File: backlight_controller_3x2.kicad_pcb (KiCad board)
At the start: 2 copper layers, 70.5 x 41.9 mm, 1 part

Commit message: Initial layout.
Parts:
- added C1: 0.1uF, backlight_controller_3x2:SM1210, B.Cu at (134.6, 102.9)
- added C2: 0.1uF, backlight_controller_3x2:SM1210, B.Cu at (125.1, 88.9)
- added C3: 0.1uF, backlight_controller_3x2:SM1210, B.Cu at (112.4, 92.7)
- added C4: 0.1uF, backlight_controller_3x2:SM1210, B.Cu at (104.8, 92.7)
- added C5: 0.1uF, backlight_controller_3x2:SM1210, B.Cu at (97.2, 92.7)
- added C6: 0.1uF, backlight_controller_3x2:SM1210, B.Cu at (89.5, 92.7)
- added D1: diode_schottky_45V_10A, backlight_controller_3x2:CFP15, B.Cu at (104.8, 75.6)
- added HPS1: BTS3256, backlight_controller_3x2:PG-TO252-5-11, B.Cu at (112.4, 89.5)
- added HPS2: BTS3256, backlight_controller_3x2:PG-TO252-5-11, B.Cu at (104.8, 89.5)
- added HPS3: BTS3256, backlight_controller_3x2:PG-TO252-5-11, B.Cu at (97.2, 89.5)
- added HPS4: BTS3256, backlight_controller_3x2:PG-TO252-5-11, B.Cu at (89.5, 89.5)
- added J1: DB9F_SMD, footprints:DB9F_SMD, F.Cu at (101.1, 88.9)
- added J2: DB9M_SMD, footprints:DB9M_SMD, F.Cu at (119.9, 88.9)
- added J3: M12-5_RCPT_F, backlight_controller_3x2:M12-5_RCPT_F, F.Cu at (151.8, 72.4)
- added J4: M12-5_RCPT_F, backlight_controller_3x2:M12-5_RCPT_F, F.Cu at (151.8, 105.4)
- added L1: LED_24V_RED, backlight_controller_3x2:LED_555-3XXX_R, F.Cu at (134.6, 88.9)
- added L10: LED_5V_GRN, backlight_controller_3x2:LED_555-3XXX_G, F.Cu at (141.6, 72.4)
- added L11: LED_5V_GRN, backlight_controller_3x2:LED_555-3XXX_G, F.Cu at (141.6, 105.4)
- added L2: LED_5V_GRN, backlight_controller_3x2:LED_555-3XXX_G, F.Cu at (134.6, 99.1)
- added L3: LED_5V_GRN, backlight_controller_3x2:LED_555-3XXX_G, F.Cu at (134.6, 96.5)
- added L4: LED_5V_GRN, backlight_controller_3x2:LED_555-3XXX_G, F.Cu at (134.6, 94.0)
- added L5: LED_5V_GRN, backlight_controller_3x2:LED_555-3XXX_G, F.Cu at (134.6, 91.4)
- added L6: LED_5V_GRN, backlight_controller_3x2:LED_555-3XXX_G, F.Cu at (134.6, 86.4)
- added L7: LED_5V_GRN, backlight_controller_3x2:LED_555-3XXX_G, F.Cu at (134.6, 83.8)
- added L8: LED_5V_GRN, backlight_controller_3x2:LED_555-3XXX_G, F.Cu at (134.6, 81.3)
- added L9: LED_5V_GRN, backlight_controller_3x2:LED_555-3XXX_G, F.Cu at (134.6, 78.7)
- added P1: MINI_FIT_JR_02X03_M_RA, backlight_controller_3x2:MINI-FIT-JR_02X03_M_RA, F.Cu at (153.7, 88.9)
- added R1: 5.9k, backlight_controller_3x2:SM1210, B.Cu at (112.4, 97.2)
- added R2: 5.9k, backlight_controller_3x2:SM1210, B.Cu at (104.8, 97.2)
- added R3: 5.9k, backlight_controller_3x2:SM1210, B.Cu at (97.2, 97.2)
- added R4: 5.9k, backlight_controller_3x2:SM1210, B.Cu at (89.5, 97.2)
- added R5: 140, backlight_controller_3x2:SM1210, B.Cu at (142.9, 81.3)
- added R6: 140, backlight_controller_3x2:SM1210, B.Cu at (142.9, 78.1)
- added R7: 140, backlight_controller_3x2:SM1210, B.Cu at (136.5, 74.3)
- added R8: 140, backlight_controller_3x2:SM1210, B.Cu at (136.5, 71.1)
- added U1: SN74ABT541BDWR, backlight_controller_3x2:SOIC_20, B.Cu at (125.1, 97.8)
- added U2: SN74ABT541BDWR, backlight_controller_3x2:SOIC_20, B.Cu at (125.1, 80.0)
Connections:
- MDB1 pad 14: (no net) -> /CHANNEL_4
- MDB1 pad 15: (no net) -> /CHANNEL_5
- MDB1 pad 16: (no net) -> /CHANNEL_6
- MDB1 pad 17: (no net) -> /CHANNEL_7
- MDB1 pad 18: (no net) -> /CHANNEL_8
- MDB1 pad 19: (no net) -> /CHANNEL_9
- MDB1 pad 2: (no net) -> /~ENABLE
- MDB1 pad 3: (no net) -> /CHANNEL_0
- MDB1 pad 4: (no net) -> /CHANNEL_1
- MDB1 pad 5: (no net) -> /CHANNEL_2
- MDB1 pad 6: (no net) -> /CHANNEL_3
- MDB1 pad GND: (no net) -> GND
- MDB1 pad VDD: (no net) -> VDD
- MDB1 pad VEE: (no net) -> VEE
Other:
- net class GND: trace_width 0.4064 -> 0.8128
- net class LEDPOWER: trace_width 0.6096 -> 0.4064
- board text added: "Janelia Modular Device backlight_controller part_number: 1271 09/2018 ver 1.0 3x2"
- board text removed: "Janelia Modular Device backlight_controller part_number: 1001 02/2017 ver 1.0 3x2"

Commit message: Finished version 1.0.
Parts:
- moved R5 27.0 mm to (135.9, 107.3), turned to 180 degrees
- moved R6 26.3 mm to (135.9, 103.5), turned to 180 degrees
- moved C1 19.8 mm to (120.7, 88.9), turned to 0 degrees
- moved L1 10.8 mm to (142.2, 96.5), turned to 270 degrees
- moved L10 8.64 mm to (134.6, 77.5), turned to 90 degrees
- moved L11 8.64 mm to (134.6, 100.3), turned to 90 degrees
- moved C2 1.91 mm to (127.0, 88.9)
- moved L4 1.27 mm to (134.6, 92.7)
- moved L7 1.27 mm to (134.6, 85.1)
- moved L9 1.27 mm to (134.6, 80.0)
- moved L2 1.27 mm to (134.6, 97.8)
- moved L3 1.27 mm to (134.6, 95.2)
- moved L5 1.27 mm to (134.6, 90.2)
- moved L6 1.27 mm to (134.6, 87.6)
- moved L8 1.27 mm to (134.6, 82.5)
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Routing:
- net GND: track 0.00 -> 283.2 mm, vias 0 -> 2
- net VAA: track 0.00 -> 149.3 mm, vias 0 -> 1
- net /~ENABLE: track 0.00 -> 117.9 mm
- net /CHANNEL_1: track 0.00 -> 91.2 mm
- net VDD: track 0.00 -> 84.8 mm
- net /CHANNEL_0: track 0.00 -> 70.1 mm, vias 0 -> 1
- net VEE: track 0.00 -> 69.2 mm
- net /CHANNEL_3: track 0.00 -> 67.1 mm, vias 0 -> 1
- net /CHANNEL_2: track 0.00 -> 67.1 mm, vias 0 -> 1
- net /backlight_3x2/C_3: track 0.00 -> 55.9 mm, vias 0 -> 1
- net /backlight_3x2/C_9: track 0.00 -> 54.3 mm, vias 0 -> 1
- net /backlight_3x2/low_power_outputs/OUTPUT_1: track 0.00 -> 54.0 mm, vias 0 -> 1
- net /backlight_3x2/low_power_outputs/OUTPUT_0: track 0.00 -> 52.7 mm, vias 0 -> 1
- net /backlight_3x2/C_2: track 0.00 -> 45.9 mm, vias 0 -> 1
- net /backlight_3x2/C_8: track 0.00 -> 39.8 mm
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- added copper zone on B.Cu, net GND
- added copper zone on F.Cu, net VAA
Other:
- net class LEDPOWER: clearance 0.254 -> 0.1016; trace_width 0.4064 -> 0.254; via_dia 0.889 -> 0.635; via_drill 0.635 -> 0.381
- net class POWER: clearance 0.254 -> 0.1016; trace_width 0.8128 -> 0.4064
- net class SIGNAL: trace_width 0.4064 -> 0.2032; via_dia 0.889 -> 0.635; via_drill 0.635 -> 0.381
- net class SUPERPOWER: clearance 0.254 -> 0.1016; trace_width 1.2192 -> 0.8128
- rule trace_min: 0.254 -> 0.2032
- rule via_min_drill: 0.508 -> 0.2032
- rule via_min_size: 0.889 -> 0.508
- board text added: "0"
- board text added: "1"
- board text added: "2"
- board text added: "3"
- board text added: "4"
- board text added: "5"
- board text added: "6"
- board text added: "7"
- board text added: "8"
- board text added: "9"
- board text added: "High Power Channels"
- board text added: "IR Backlight"
- board text added: "Low Power Channels"
- board text added: "Visible Backlight"

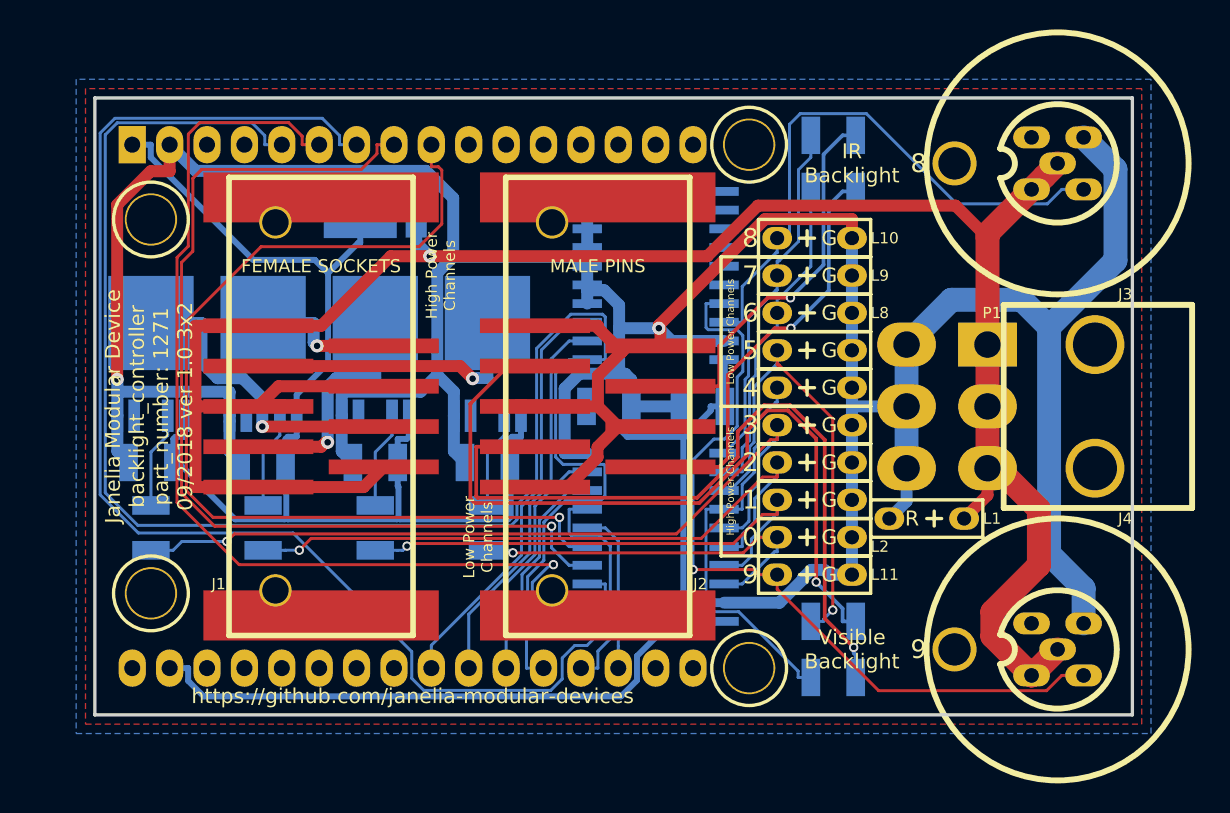
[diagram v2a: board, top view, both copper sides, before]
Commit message: Moved some pcb text.
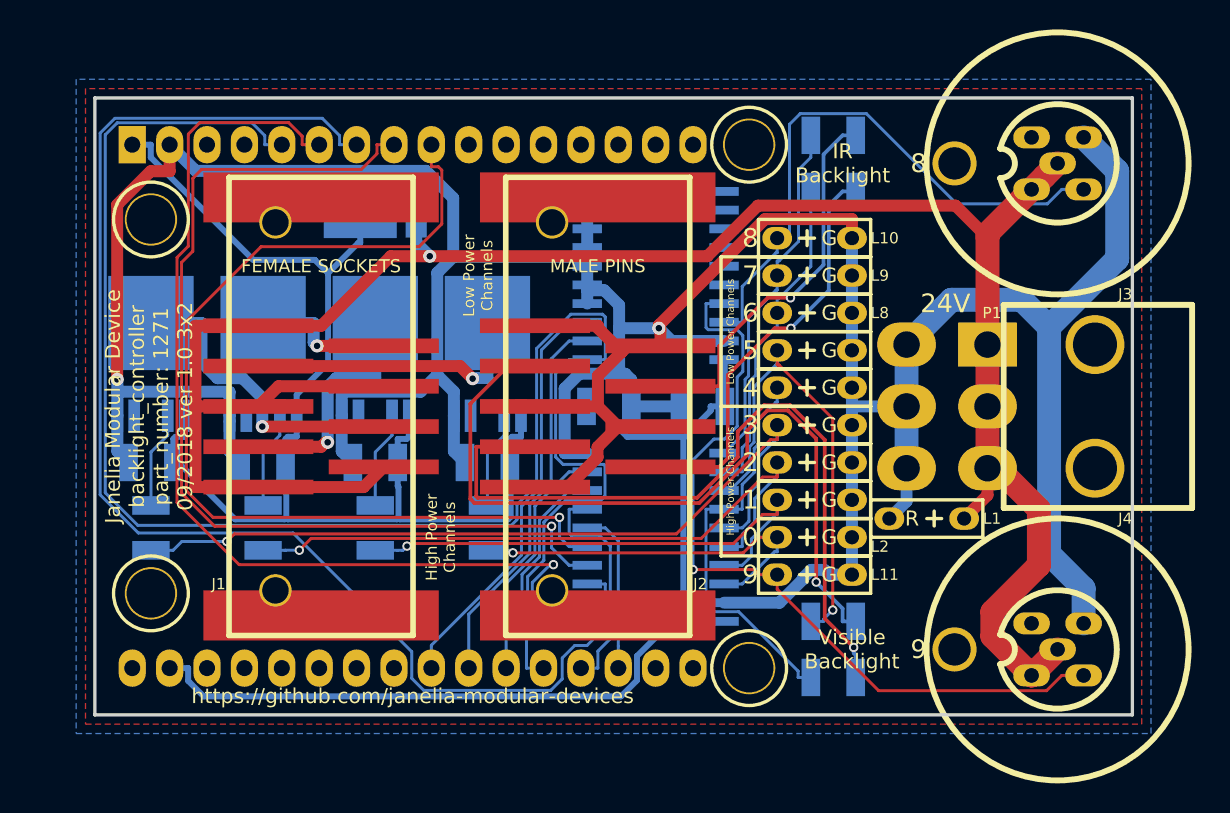
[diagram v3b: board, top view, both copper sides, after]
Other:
- board text added: "24V"
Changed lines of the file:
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@@
-(kicad_pcb (version 20171130) (host pcbnew 6.0.0-rc1-unknown-ba8647f~66~ubuntu18.04.1)
+(kicad_pcb (version 20171130) (host pcbnew 6.0.0-rc1-unknown-ab92882~66~ubuntu18.04.1)
   (general
     (thickness 1.6)
-    (drawings 28)
+    (drawings 29)
     (tracks 601)
     (zones 0)
@@
       (net 1 VEE) (solder_mask_margin 0.07) (clearance 0.07))
   )
+  (gr_text 24V (at 143.51 81.915) (layer F.SilkS)
+    (effects (font (size 1.27 1.27) (thickness 0.3175)))
+  )
   (gr_text "Visible\nBacklight" (at 137.16 105.41) (layer F.SilkS)
     (effects (font (size 1.016 1.016) (thickness 0.254)))
   )
-  (gr_text "IR\nBacklight" (at 137.16 72.39) (layer F.SilkS)
+  (gr_text "IR\nBacklight" (at 136.525 72.39) (layer F.SilkS)
     (effects (font (size 1.016 1.016) (thickness 0.254)))
   )
-  (gr_text "Low Power\nChannels" (at 111.76 97.79 90) (layer F.SilkS)
+  (gr_text "Low Power\nChannels" (at 111.76 80.01 90) (layer F.SilkS)
     (effects (font (size 0.762 0.762) (thickness 0.1905)))
   )
-  (gr_text "High Power\nChannels" (at 109.22 80.01 90) (layer F.SilkS)
+  (gr_text "High Power\nChannels" (at 109.22 97.79 90) (layer F.SilkS)
     (effects (font (size 0.762 0.762) (thickness 0.1905)))
   )
@@
   (segment (start 152.8978 70.6222) (end 152.898 70.6222) (width 0.8128) (layer B.Cu) (net 2))
   (segment (start 152.8978 103.6422) (end 152.898 103.642) (width 0.8128) (layer B.Cu) (net 2))
-  (segment (start 152.898 70.6222) (end 155.062 72.7866) (width 1.6256) (layer B.Cu) (net 2))
-  (segment (start 155.062 72.7866) (end 155.062 78.9945) (width 1.6256) (layer B.Cu) (net 2))
-  (segment (start 155.062 78.9945) (end 150.552 83.5051) (width 1.6256) (layer B.Cu) (net 2))
   (segment (start 119.175 79.375) (end 119.175 80.645) (width 0.8128) (layer B.Cu) (net 2))
   (segment (start 137.16 82.55) (end 137.16 85.09) (width 0.8128) (layer B.Cu) (net 2))
@@
   (via (at 124.0413 83.5869) (size 0.889) (layers F.Cu B.Cu) (net 2))
   (via (at 87.2428 87.0621) (size 0.889) (layers F.Cu B.Cu) (net 2))
+  (segment (start 155.18129 78.87581) (end 150.552 83.5051) (width 1.6256) (layer B.Cu) (net 2))
+  (segment (start 152.898 70.6222) (end 155.18129 72.90549) (width 1.6256) (layer B.Cu) (net 2))
+  (segment (start 155.18129 72.90549) (end 155.18129 78.87581) (width 1.6256) (layer B.Cu) (net 2))
   (segment (start 98.7302 96.4696) (end 98.7302 94.3614) (width 0.4064) (layer B.Cu) (net 3))
   (segment (start 98.7302 94.3614) (end 98.679 94.3102) (width 0.4064) (layer B.Cu) (net 3))

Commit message: Changes towards v1.1.
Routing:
- net GND: track 283.3 -> 0.00 mm, vias 2 -> 0
- net VAA: track 149.3 -> 0.00 mm, vias 1 -> 0
- net /~ENABLE: track 117.9 -> 0.00 mm
- net /CHANNEL_1: track 91.2 -> 0.00 mm
- net VDD: track 84.8 -> 0.00 mm
- net /CHANNEL_0: track 70.1 -> 0.00 mm, vias 1 -> 0
- net VEE: track 69.2 -> 0.00 mm
- net /CHANNEL_3: track 67.1 -> 0.00 mm, vias 1 -> 0
- net /CHANNEL_2: track 67.1 -> 0.00 mm, vias 1 -> 0
- net /backlight_3x2/C_3: track 55.9 -> 0.00 mm, vias 1 -> 0
- net /backlight_3x2/C_9: track 54.3 -> 0.00 mm, vias 1 -> 0
- net /backlight_3x2/low_power_outputs/OUTPUT_1: track 54.0 -> 0.00 mm, vias 1 -> 0
- net /backlight_3x2/low_power_outputs/OUTPUT_0: track 52.7 -> 0.00 mm, vias 1 -> 0
- net /backlight_3x2/C_2: track 45.9 -> 0.00 mm, vias 1 -> 0
- net /backlight_3x2/C_8: track 39.8 -> 0.00 mm
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- removed copper zone on B.Cu, net GND
- removed copper zone on F.Cu, net VAA
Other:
- board text added: "Janelia Modular Device backlight_controller part_number: 1271 10/2018 ver 1.1 3x2"
- board text removed: "Janelia Modular Device backlight_controller part_number: 1271 09/2018 ver 1.0 3x2"

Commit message: Finished version 1.1.
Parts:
- added U3: NUD3124, backlight_controller_3x2:TO-236-3, B.Cu at (148.6, 75.6)
- added U4: NUD3124, backlight_controller_3x2:TO-236-3, B.Cu at (148.6, 102.2)
- J3, J4: value M12-5_RCPT_F -> M12-5-RCPT_F_SMD; footprint backlight_controller_3x2:M12-5_RCPT_F -> footprints:M12-5_RCPT_F_SMD
- moved J3 2.54 mm to (148.6, 72.4), turned to 0 degrees
- moved J4 2.54 mm to (148.6, 105.4), turned to 0 degrees
- moved J2 1.78 mm to (118.1, 88.9)
- moved J1 0.76 mm to (100.3, 88.9)
- moved C1 0.64 mm to (120.0, 88.9)
- moved C2 0.64 mm to (126.4, 88.9)
- moved U1 0.64 mm to (123.2, 97.8)
- moved U2 0.64 mm to (123.2, 80.0)
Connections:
- J3 pad 2: (no net) -> /backlight_3x2/backlight_outputs/ir/NPN
- J3 pad 4: /backlight_3x2/C_8 -> (no net)
- J4 pad 2: (no net) -> /backlight_3x2/backlight_outputs/visible/NPN
- J4 pad 4: /backlight_3x2/C_9 -> (no net)
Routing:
- net GND: track 0.00 -> 331.0 mm, vias 0 -> 1
- net VAA: track 0.00 -> 124.0 mm, vias 0 -> 1
- net VDD: track 0.00 -> 117.6 mm
- net /~ENABLE: track 0.00 -> 109.7 mm
- net /CHANNEL_0: track 0.00 -> 80.4 mm, vias 0 -> 1
- net VEE: track 0.00 -> 71.0 mm
- net /CHANNEL_3: track 0.00 -> 69.6 mm, vias 0 -> 1
- net /CHANNEL_2: track 0.00 -> 61.8 mm, vias 0 -> 2
- net /backlight_3x2/C_3: track 0.00 -> 57.1 mm, vias 0 -> 1
- net /backlight_3x2/C_9: track 0.00 -> 52.1 mm, vias 0 -> 1
- net /backlight_3x2/low_power_outputs/OUTPUT_0: track 0.00 -> 47.2 mm, vias 0 -> 1
- net /backlight_3x2/C_2: track 0.00 -> 46.4 mm, vias 0 -> 1
- net /CHANNEL_8: track 0.00 -> 46.0 mm, vias 0 -> 1
- net /CHANNEL_1: track 0.00 -> 45.0 mm, vias 0 -> 3
- net /backlight_3x2/low_power_outputs/OUTPUT_1: track 0.00 -> 42.3 mm, vias 0 -> 3
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- added copper zone on B.Cu, net GND
- added copper zone on F.Cu, net VAA

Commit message: high_power -> high_voltage. low_power -> low_voltage.
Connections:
- net /backlight_3x2/high_power_outputs/OUTPUT_0 renamed /backlight_3x2/high_voltage_outputs/OUTPUT_0
- net /backlight_3x2/high_power_outputs/OUTPUT_1 renamed /backlight_3x2/high_voltage_outputs/OUTPUT_1
- net /backlight_3x2/high_power_outputs/OUTPUT_2 renamed /backlight_3x2/high_voltage_outputs/OUTPUT_2
- net /backlight_3x2/high_power_outputs/OUTPUT_3 renamed /backlight_3x2/high_voltage_outputs/OUTPUT_3
- net /backlight_3x2/high_power_outputs/high_power_output_0/FAULT renamed /backlight_3x2/high_voltage_outputs/high_voltage_output_0/FAULT
- net /backlight_3x2/high_power_outputs/high_power_output_1/FAULT renamed /backlight_3x2/high_voltage_outputs/high_voltage_output_1/FAULT
- net /backlight_3x2/high_power_outputs/high_power_output_2/FAULT renamed /backlight_3x2/high_voltage_outputs/high_voltage_output_2/FAULT
- net /backlight_3x2/high_power_outputs/high_power_output_3/FAULT renamed /backlight_3x2/high_voltage_outputs/high_voltage_output_3/FAULT
- net /backlight_3x2/low_power_outputs/OUTPUT_0 renamed /backlight_3x2/low_voltage_outputs/OUTPUT_0
- net /backlight_3x2/low_power_outputs/OUTPUT_1 renamed /backlight_3x2/low_voltage_outputs/OUTPUT_1
- net /backlight_3x2/low_power_outputs/OUTPUT_2 renamed /backlight_3x2/low_voltage_outputs/OUTPUT_2
- net /backlight_3x2/low_power_outputs/OUTPUT_3 renamed /backlight_3x2/low_voltage_outputs/OUTPUT_3

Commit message: Progress towards v1.2.
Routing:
- net GND: track 331.0 -> 0.00 mm, vias 1 -> 0
- net VAA: track 124.0 -> 0.00 mm, vias 1 -> 0
- net VDD: track 117.6 -> 0.00 mm
- net /~ENABLE: track 109.7 -> 0.00 mm
- net /CHANNEL_0: track 80.4 -> 0.00 mm, vias 1 -> 0
- net VEE: track 71.0 -> 0.00 mm
- net /CHANNEL_3: track 69.6 -> 0.00 mm, vias 1 -> 0
- net /CHANNEL_2: track 61.8 -> 0.00 mm, vias 2 -> 0
- net /backlight_3x2/C_3: track 57.1 -> 0.00 mm, vias 1 -> 0
- net /backlight_3x2/C_9: track 52.1 -> 0.00 mm, vias 1 -> 0
- net /backlight_3x2/low_voltage_outputs/OUTPUT_0: track 47.2 -> 0.00 mm, vias 1 -> 0
- net /backlight_3x2/C_2: track 46.4 -> 0.00 mm, vias 1 -> 0
- net /CHANNEL_8: track 46.0 -> 0.00 mm, vias 1 -> 0
- net /CHANNEL_1: track 45.0 -> 0.00 mm, vias 3 -> 0
- net /backlight_3x2/low_voltage_outputs/OUTPUT_1: track 42.3 -> 0.00 mm, vias 3 -> 0
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- removed copper zone on B.Cu, net GND
- removed copper zone on F.Cu, net VAA
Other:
- board text added: "High Voltage Channels"
- board text added: "Janelia Modular Device backlight_controller part_number: 1271 10/2018 ver 1.2 3x2"
- board text added: "Low Voltage Channels"
- board text removed: "High Power Channels"
- board text removed: "Janelia Modular Device backlight_controller part_number: 1271 10/2018 ver 1.1 3x2"
- board text removed: "Low Power Channels"

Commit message: Finished v1.2 schematic.
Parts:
- R5, R6, R7, R8: value 140 -> 75; footprint backlight_controller_3x2:SM1210 -> footprints:SM0805
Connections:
- MDB1 pad 10: (no net) -> /CHANNEL_5
- MDB1 pad 14: /CHANNEL_4 -> (no net)
- MDB1 pad 15: /CHANNEL_5 -> (no net)
- MDB1 pad 16: /CHANNEL_6 -> (no net)
- MDB1 pad 17: /CHANNEL_7 -> (no net)
- MDB1 pad 18: /CHANNEL_8 -> (no net)
- MDB1 pad 19: /CHANNEL_9 -> (no net)
- MDB1 pad 20: (no net) -> /CHANNEL_6
- MDB1 pad 21: (no net) -> /CHANNEL_7
- MDB1 pad 22: (no net) -> /CHANNEL_8
- MDB1 pad 23: (no net) -> /CHANNEL_9
- MDB1 pad 9: (no net) -> /CHANNEL_4
